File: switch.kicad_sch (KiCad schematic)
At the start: 82 parts, among them SW1 ESC, SW10 F9, SW11 F10, SW12 F11, SW13 F12, SW14 DEL, SW15 ², SW16 1, SW17 2, SW18 3, SW19 4, SW2 F1, SW20 5, SW21 6, SW22 7, SW23 8, SW24 9, SW25 0, SW26 °, SW27 +, SW28 BACKSPACE, SW29 PG-UP, SW3 F2, SW30 A, SW31 Z, SW32 R, SW33 T, SW34 Y, SW35 U, SW36 I, SW37 O, SW38 P, SW39 ¨, SW4 F3, SW40 £, SW41 PG-DOWN, SW5 F4, SW6 F5, SW7 F6, SW73 Spacebar, SW74 TAB, SW75 Backspace, SW76 Caps Lock, SW77 L-Shift, SW78 L-Ctrl, SW79 L-Win, SW8 F7, SW80 Alt, SW81 R-Shift, SW82 Enter, SW9 F8

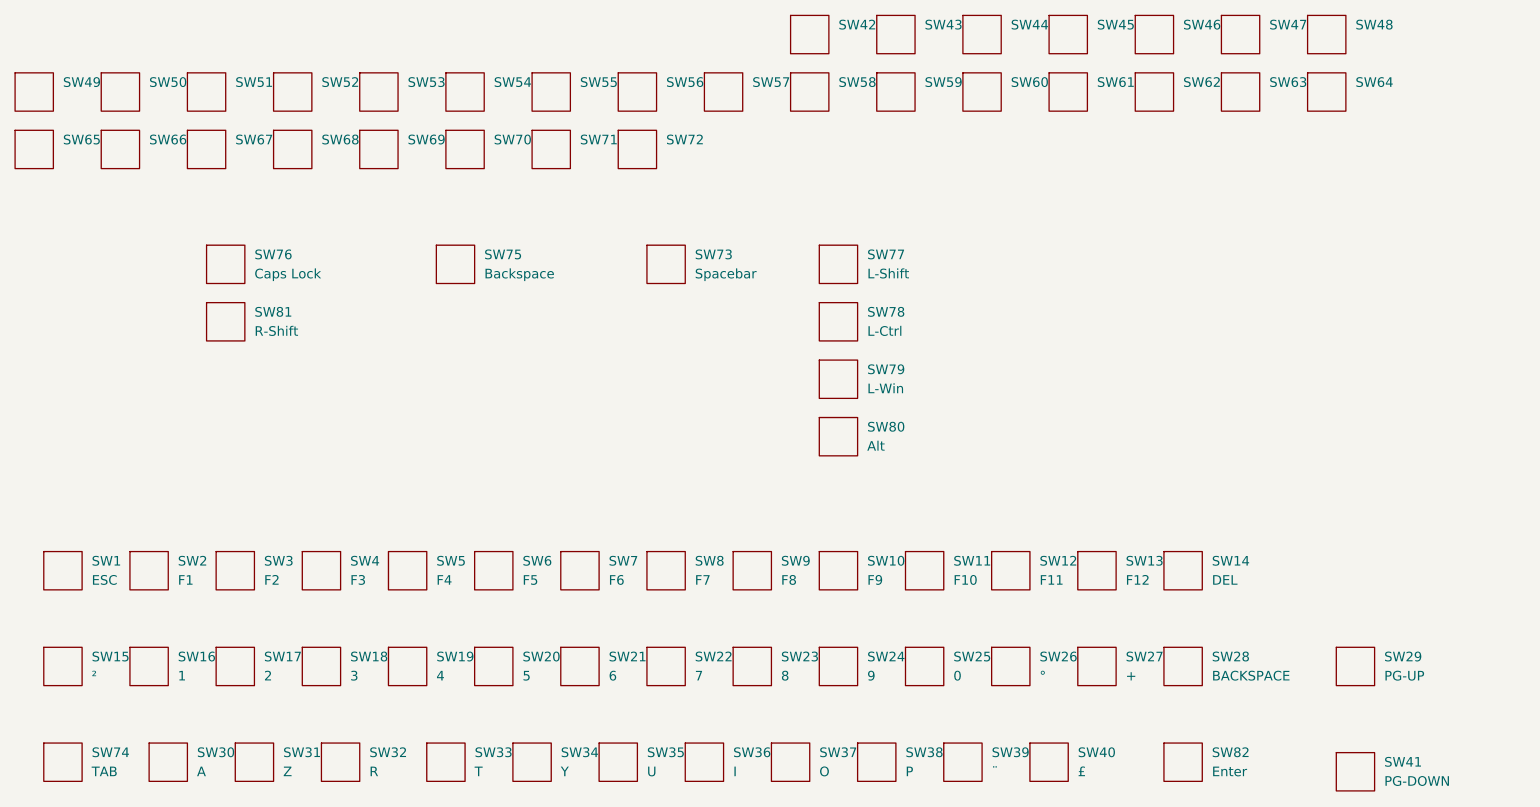
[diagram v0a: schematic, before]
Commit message: start keyboard switch layout
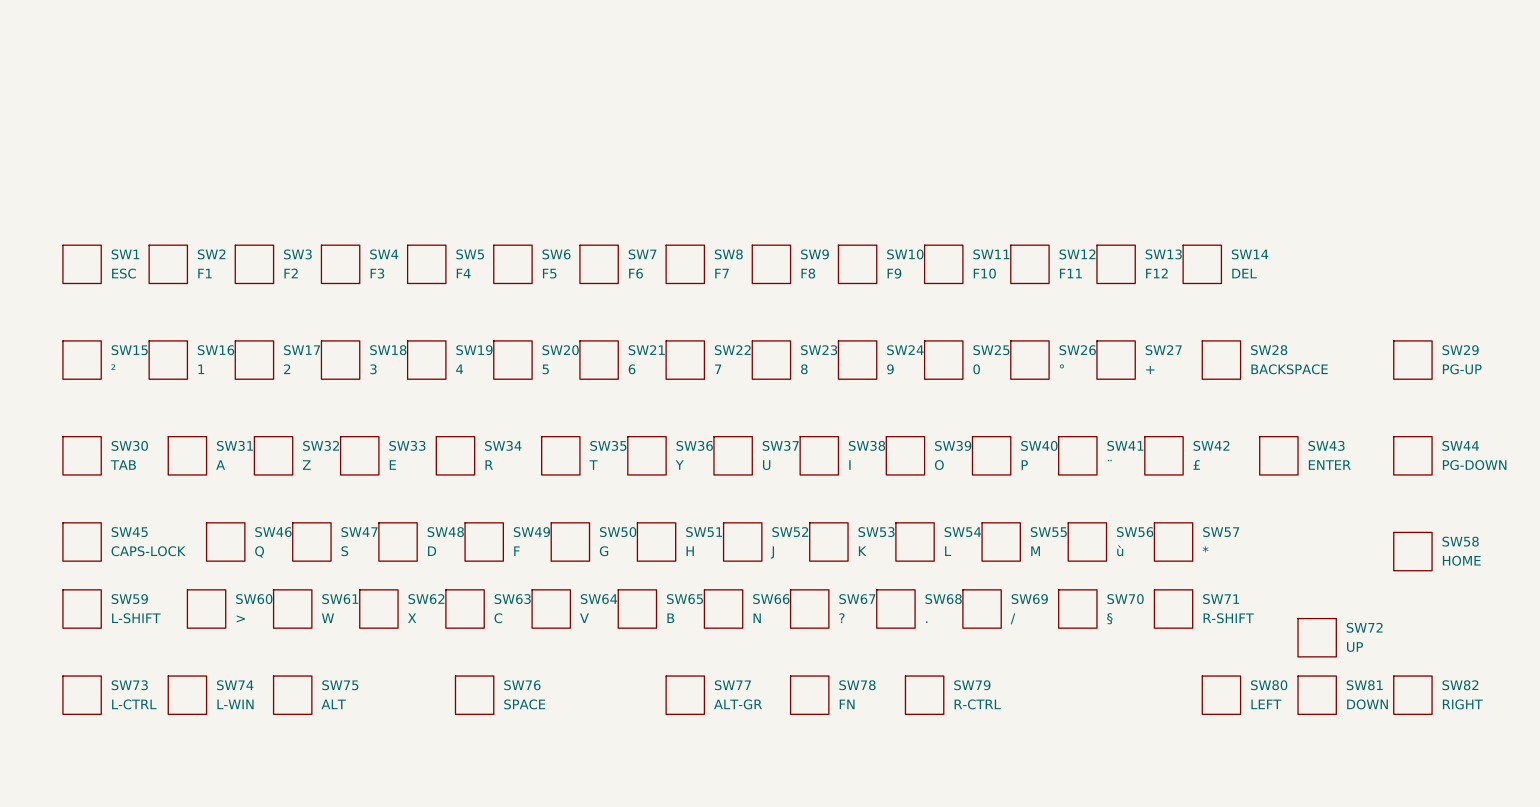
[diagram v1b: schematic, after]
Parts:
- SW28: renamed from SW75; value Backspace -> BACKSPACE
- SW33: renamed from SW68; value ~ -> E
- SW43: renamed from SW82; value Enter -> ENTER; footprint 75HE:Switch_1U -> 75HE:Switch_ENTER_ISO
- SW45: renamed from SW76; value Caps Lock -> CAPS-LOCK
- SW46: renamed from SW42; value ~ -> Q
- SW47: renamed from SW43; value ~ -> S
- SW48: renamed from SW44; value ~ -> D
- SW49: renamed from SW45; value ~ -> F
- SW50: renamed from SW46; value ~ -> G
- SW51: renamed from SW47; value ~ -> H
- SW52: renamed from SW48; value ~ -> J
- SW53: renamed from SW49; value ~ -> K
- SW54: renamed from SW50; value ~ -> L
- SW55: renamed from SW51; value ~ -> M
- SW56: renamed from SW52; value ~ -> ù
- SW57: renamed from SW53; value ~ -> *
- SW58: renamed from SW54; value ~ -> HOME
- SW59: renamed from SW77; value L-Shift -> L-SHIFT
- SW60: renamed from SW55; value ~ -> >
- SW61: renamed from SW56; value ~ -> W
- SW62: renamed from SW57; value ~ -> X
- SW63: renamed from SW58; value ~ -> C
- SW64: renamed from SW59; value ~ -> V
- SW65: renamed from SW60; value ~ -> B
- SW66: renamed from SW61; value ~ -> N
- SW67: renamed from SW62; value ~ -> ?
- SW68: renamed from SW63; value ~ -> .
- SW69: renamed from SW64; value ~ -> /
- SW70: renamed from SW28; value BACKSPACE -> §
- SW71: renamed from SW81; value R-Shift -> R-SHIFT
- SW72: renamed from SW69; value ~ -> UP
- SW73: renamed from SW78; value L-Ctrl -> L-CTRL
- SW74: renamed from SW79; value L-Win -> L-WIN
- SW75: renamed from SW80; value Alt -> ALT
- SW76: renamed from SW73; value Spacebar -> SPACE
- SW77: renamed from SW65; value ~ -> ALT-GR
- SW78: renamed from SW66; value ~ -> FN
- SW79: renamed from SW67; value ~ -> R-CTRL
- SW80: renamed from SW70; value ~ -> LEFT
- SW81: renamed from SW71; value ~ -> DOWN
- SW82: renamed from SW72; value ~ -> RIGHT
- renumbered SW74 to SW30, SW30 to SW31, SW31 to SW32, SW32 to SW34, SW33 to SW35, SW34 to SW36, SW35 to SW37, SW36 to SW38, SW37 to SW39, SW38 to SW40, SW39 to SW41, SW40 to SW42, SW41 to SW44
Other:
- moved on the sheet: SW1, SW10, SW11, SW12, SW13, SW14, SW15, SW16, SW17, SW18, SW19, SW2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

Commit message: clean schematics
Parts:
- SW1, SW10, SW11, SW12, SW13, SW14, SW15, SW16, SW17, SW18, SW19, SW2, SW20, SW21, SW22, SW23, SW24, SW25, SW26, SW27, SW28, SW29, SW3, SW30, SW31, SW32, SW33, SW34, SW35, SW36, SW37, SW38, SW39, SW4, SW40, SW41, SW42, SW43, SW44, SW45, SW46, SW47, SW48, SW49, SW5, SW50, SW51, SW52, SW53, SW54, SW55, SW56, SW57, SW58, SW59, SW6, SW60, SW61, SW62, SW63, SW64, SW65, SW66, SW67, SW68, SW69, SW7, SW70, SW71, SW72, SW73, SW74, SW75, SW76, SW77, SW78, SW79, SW8, SW80, SW81, SW82, SW9: now left out of the parts list

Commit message: Add gitattributes, update ignores, tidy PCB/libs
Normalize project files and clean up repository: add .gitattributes for KiCad text files and update .gitignore to exclude backups, generated outputs and production artifacts. Remove many large binary backups and unused images/zips to reduce repo clutter. Add Assets images, multiple 3D models and KiCad library footprints/symbols (new Library and PCM_JLCPCB entries), and legacy project exports. Update 75he.kicad_pcb to use ${KIPRJMOD} model paths, remove redundant units/zone_defaults blocks, simplify switch attributes, hide heavy 3D models, and make small footprint fixes (fp_poly -> fp_rect, pad coordinate precision and UUID updates). Also add README and adjust fp-lib-table, sym-lib-table and switch schematic file.
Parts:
- SW1, SW10, SW11, SW12, SW13, SW14, SW15, SW16, SW17, SW18, SW19, SW2, SW20, SW21, SW22, SW23, SW24, SW25, SW26, SW27, SW29, SW3, SW31, SW32, SW33, SW34, SW35, SW36, SW37, SW38, SW39, SW4, SW40, SW41, SW42, SW43, SW44, SW46, SW47, SW48, SW49, SW5, SW50, SW51, SW52, SW53, SW54, SW55, SW56, SW57, SW58, SW6, SW60, SW61, SW62, SW63, SW64, SW65, SW66, SW67, SW68, SW69, SW7, SW70, SW72, SW77, SW78, SW79, SW8, SW80, SW81, SW82, SW9: symbol 70HE:Switch_1U -> 75HE:Switch_1U
- SW28: symbol 70HE:Switch_2U -> 75HE:Switch_2U
- SW30: symbol 70HE:Switch_1.5U -> 75HE:Switch_1.5U
- SW45, SW71: symbol 70HE:Switch_1.75U -> 75HE:Switch_1.75U
- SW59, SW73, SW74, SW75: symbol 70HE:Switch_1.25U -> 75HE:Switch_1.25U
- SW76: symbol 70HE:Switch_6.25U -> 75HE:Switch_6.25U
